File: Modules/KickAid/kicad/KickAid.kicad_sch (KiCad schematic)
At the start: 123 parts, among them Q1 BCM847BS, U1 TL074, U2 TL074, U3 TL074, U4 TL074, U5 TL074, U6 LM324, U7 LM358, U8 74HC04, U9 78L05

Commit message: Update KickAid PCBs.
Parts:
- C22: value 100pF -> 47pF
- R10: value 10k -> 15k
- R27: value 160k -> 120k
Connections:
- net GND: now also J_IN1.SW
- no-connect marks 11 -> 10

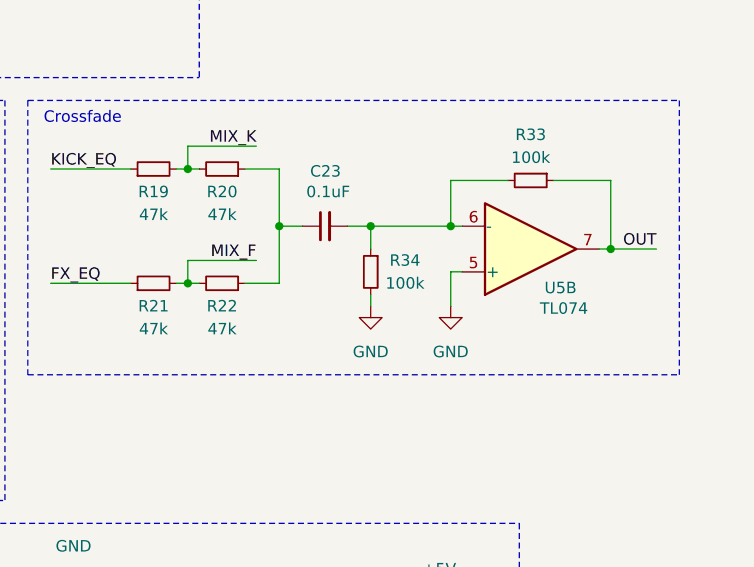
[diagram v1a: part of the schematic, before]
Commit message: Change a resistor on KickAid for better AC coupling.
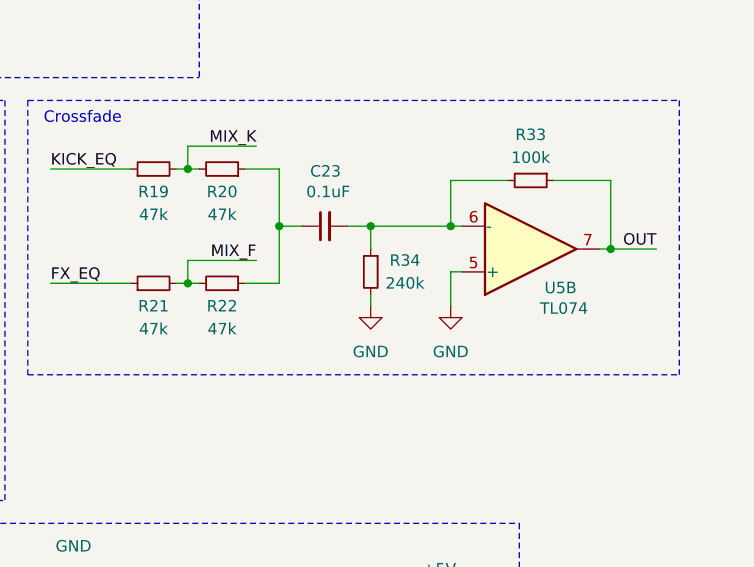
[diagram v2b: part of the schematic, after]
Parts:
- R34: value 100k -> 240k
